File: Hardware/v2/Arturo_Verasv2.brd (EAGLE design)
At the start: 59.8 x 82.4 mm, 31 parts, among them T3 2SC1815, T4 2SC1815, T6 2SC1815, T7 2SC1815

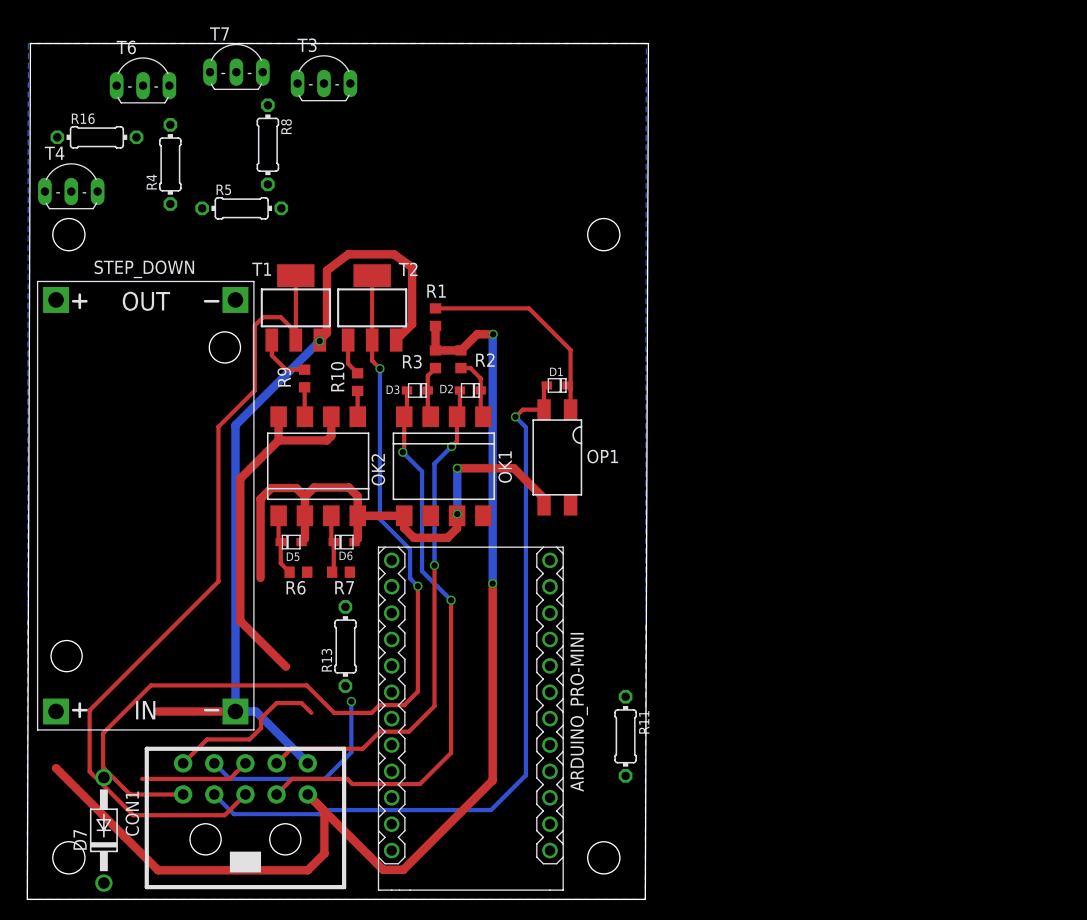
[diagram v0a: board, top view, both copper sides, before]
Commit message: hardware update
se agregan más componentes
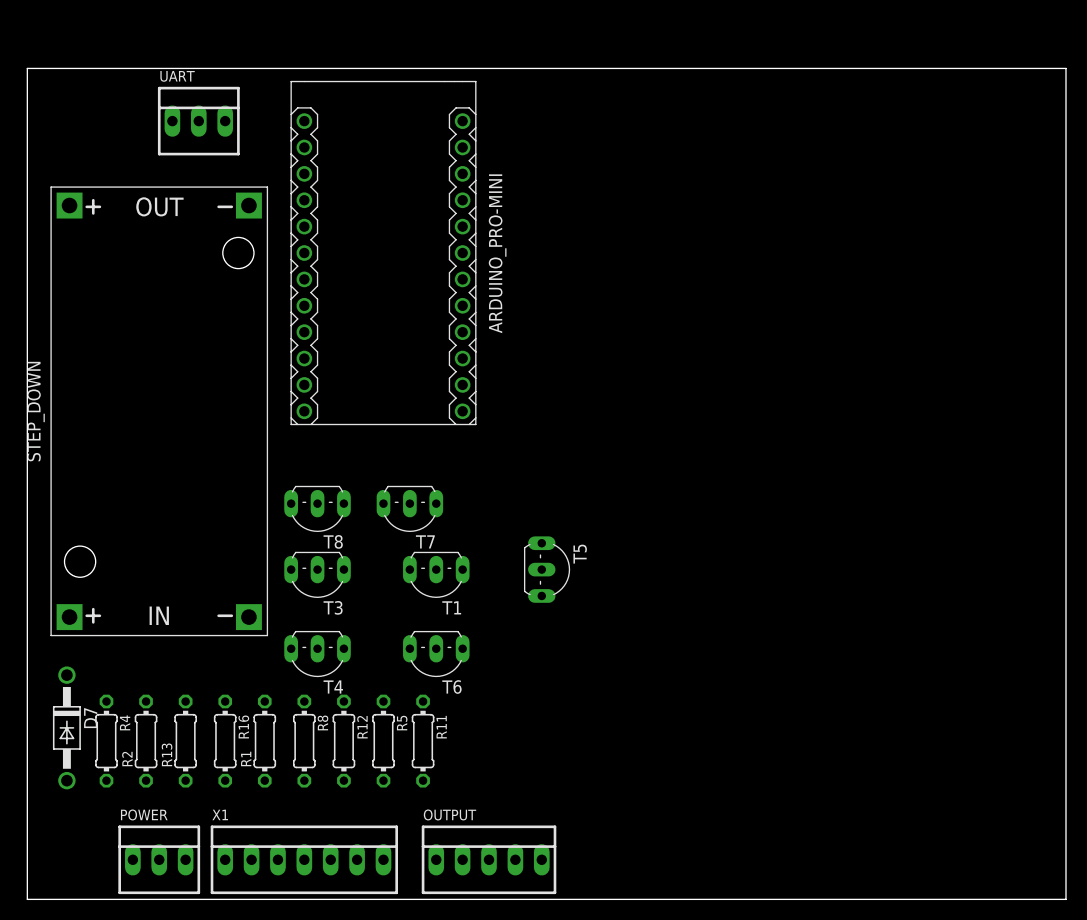
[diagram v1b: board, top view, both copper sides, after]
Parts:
- removed CON1: (no value), ArturoVeras:MICRO_MATE_N_LOK_TRUEHOLE_10POS
- removed D1, D2, D3, D5, D6: (no value), adafruit:SOD-323F
- removed OK1, OK2: LTV826S, optocoupler:DIL8-SMD
- removed OP1: LTV816S, ArturoVeras:SMD4
- removed R10, R6, R7, R9: 1k, rcl:R0603
- removed R3: 10k, rcl:R0603
- removed T2: (no value), ArturoVeras:SOT223
- added OUTPUT: 22-23-2051, con-molex:22-23-2051
- added POWER, UART: 22-23-2031, con-molex:22-23-2031
- added R12: 3k3, resistor:0204/7
- added T5, T8: 2SC1815, transistor:TO92-ECB
- added X1: 22-23-2071, con-molex:22-23-2071
- R1, R2: value 10k -> 330; device rcl:R0603 -> resistor:0204/7
- R13: value 47k -> 330
- T1: value (none) -> 2SC1815; device ArturoVeras:SOT223 -> transistor:TO92-ECB
- moved T6 61.1 mm to (39.4, 24.1), turned to 180 degrees
- moved R16 59.4 mm to (19.1, 15.2), turned to 270 degrees
- moved R8 57.5 mm to (26.7, 15.2)
- moved R4 55.9 mm to (7.62, 15.2), turned to 270 degrees
- moved R5 53.1 mm to (34.3, 15.2), turned to 270 degrees
- moved T4 50.0 mm to (27.9, 24.1), turned to 180 degrees
- moved R2 47.7 mm to (11.4, 15.2), turned to 90 degrees
- moved T3 46.8 mm to (27.9, 31.8), turned to 180 degrees
- moved ARDUINO_PRO-MINI 45.6 mm to (34.3, 62.2), turned to 270 degrees
- moved T7 44.8 mm to (36.8, 38.1), turned to 180 degrees
- moved R1 44.0 mm to (22.9, 15.2)
- moved T1 28.6 mm to (39.4, 31.8), turned to 180 degrees
- moved R11 19.5 mm to (38.1, 15.2)
- moved R13 17.9 mm to (15.2, 15.2)
- moved D7 10.5 mm to (3.81, 16.5), turned to 270 degrees
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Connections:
- net DTDIN2_OUT renamed DTDIN2_OUT-
- net N$21 renamed DLED_OUTPUT
- removed net 1-WIREIN: CON1.8
- removed net 1-WIREOUT: CON1.6
- removed net 1-WIREPOWER: CON1.10
- removed net BUZZER-: T6.C
- removed net CC_OUT: CON1.9, T2.2, T2.4
- removed net DOORIN: CON1.3, D3.A, OK1.4
- removed net DTDOUT1_IN: T7.C
- removed net DTDOUT2_IN: ARDUINO_PRO-MINI.J7.8
- removed net DTOUT1_IN: ARDUINO_PRO-MINI.J7.5
- removed net GIN: CON1.7, D1.A, OP1.2
- removed net GNDMIC: D5.A, D6.A, OK1.5, OK1.7, OK2.2, OK2.4, OP1.3
- removed net JAMIN: CON1.4, D2.A, OK1.2
- removed net LED+: R5.1
- removed net LED-: T4.C
- removed net N$10: ARDUINO_PRO-MINI.J7.1, OK1.6
- removed net N$11: OK2.7, R9.1
- removed net N$13: D5.C, OK2.1, R6.2
- removed net N$15: D6.C, OK2.3, R7.2
- removed net N$16: OK2.5, R10.1
- removed net N$17: R9.2, T1.1
- removed net N$18: R10.2, T2.1
- removed net N$24: ARDUINO_PRO-MINI.J6.3
- removed net SPKEAR_OUT: CON1.5, T1.2, T1.4
- removed net TDIN2_OUT: R16.2, T3.E
- removed net TDOUT1_IN: R8.2
- removed net VCCMIC: ARDUINO_PRO-MINI.J6.4, OK2.6, OK2.8
- new net BUZZER_OUTPUT-: OUTPUT.2, T6.C
- new net CC_OUTPUT-: OUTPUT.1, T8.C
- new net DDOOR_INPUT-: ARDUINO_PRO-MINI.J7.1, X1.6
- new net DENABLEDOOR_INPUT-: ARDUINO_PRO-MINI.J7.4, X1.5
- new net DGENERAL_INPUT: ARDUINO_PRO-MINI.J7.5, T5.C
- new net DIGNITION_INPUT: ARDUINO_PRO-MINI.J7.2, T7.C
- new net DJAMMINGAUX_INPUT-: ARDUINO_PRO-MINI.J7.7, X1.4
- new net DTDOUT1_INPUT-: ARDUINO_PRO-MINI.J7.6, X1.3
- new net DTDOUT2_INPUT-: ARDUINO_PRO-MINI.J7.8, X1.1
- new net GENERAL_INPUT+: R12.2, X1.7
- new net IGNITION_INPUT+: R8.2, X1.2
- new net LED_OUTPUT-: OUTPUT.4, R5.2
- new net N$1: R12.1, T5.B
- new net SPEAKER_OUTPUT-: OUTPUT.3, T1.C
- new net TDIN2_OUTPUT+: OUTPUT.5, R16.2, T3.E
- new net VCC: ARDUINO_PRO-MINI.J6.4, POWER.3
- net DCC_OUT: now also R1.1; no longer R7.1
- net DSPEAKER_OUT: now also R2.1; no longer R6.1
- net GND: now also POWER.2, T1.E, T5.E, T8.E; no longer ARDUINO_PRO-MINI.J7.9, CON1.2, T1.3, T2.3
- net N$3: now also R1.2, T8.B; no longer ARDUINO_PRO-MINI.J7.4, OP1.4
- net N$4: now also R2.2, T1.B; no longer D1.C, OP1.1, R1.2
- net N$6: now also R5.1, T4.C; no longer D2.C, OK1.1, R2.2
- net N$7: now also ARDUINO_PRO-MINI.J7.12, UART.3; no longer ARDUINO_PRO-MINI.J7.2, OK1.8
- net N$8: now also ARDUINO_PRO-MINI.J7.11, UART.2; no longer D3.C, OK1.3, R3.2
- net N$9: now also ARDUINO_PRO-MINI.J7.9, UART.1; no longer ARDUINO_PRO-MINI.J7.10
- net VIN: now also POWER.1; no longer CON1.1, R1.1, R2.1, R3.1, R5.2
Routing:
- net VIN: track 112.8 -> 0.00 mm, vias 2 -> 0
- net CC_OUT: track 88.1 -> 0.00 mm, vias 2 -> 0
- net GND: track 79.4 -> 0.00 mm, vias 1 -> 0
- net SPKEAR_OUT: track 78.2 -> 0.00 mm
- net GIN: track 72.7 -> 0.00 mm, vias 1 -> 0
- net DOORIN: track 55.9 -> 0.00 mm, vias 2 -> 0
- net GNDMIC: track 55.0 -> 0.00 mm, vias 2 -> 0
- net JAMIN: track 48.9 -> 0.00 mm, vias 2 -> 0
- net VCCMIC: track 34.5 -> 0.00 mm
- net N$4: track 20.8 -> 0.00 mm
- net 1-WIREIN: track 19.8 -> 0.00 mm, vias 1 -> 0
- net 1-WIREPOWER: track 15.7 -> 0.00 mm
- net 1-WIREOUT: track 10.6 -> 0.00 mm
- net N$6: track 6.10 -> 0.00 mm
- net N$13: track 5.87 -> 0.00 mm
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- removed copper zone on layer 16, net GNDMIC
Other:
- board size 59.8 x 82.4 mm -> 100 x 80 mm
